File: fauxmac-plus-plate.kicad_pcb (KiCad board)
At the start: 2 copper layers, 86.5 x 89 mm, 4 parts

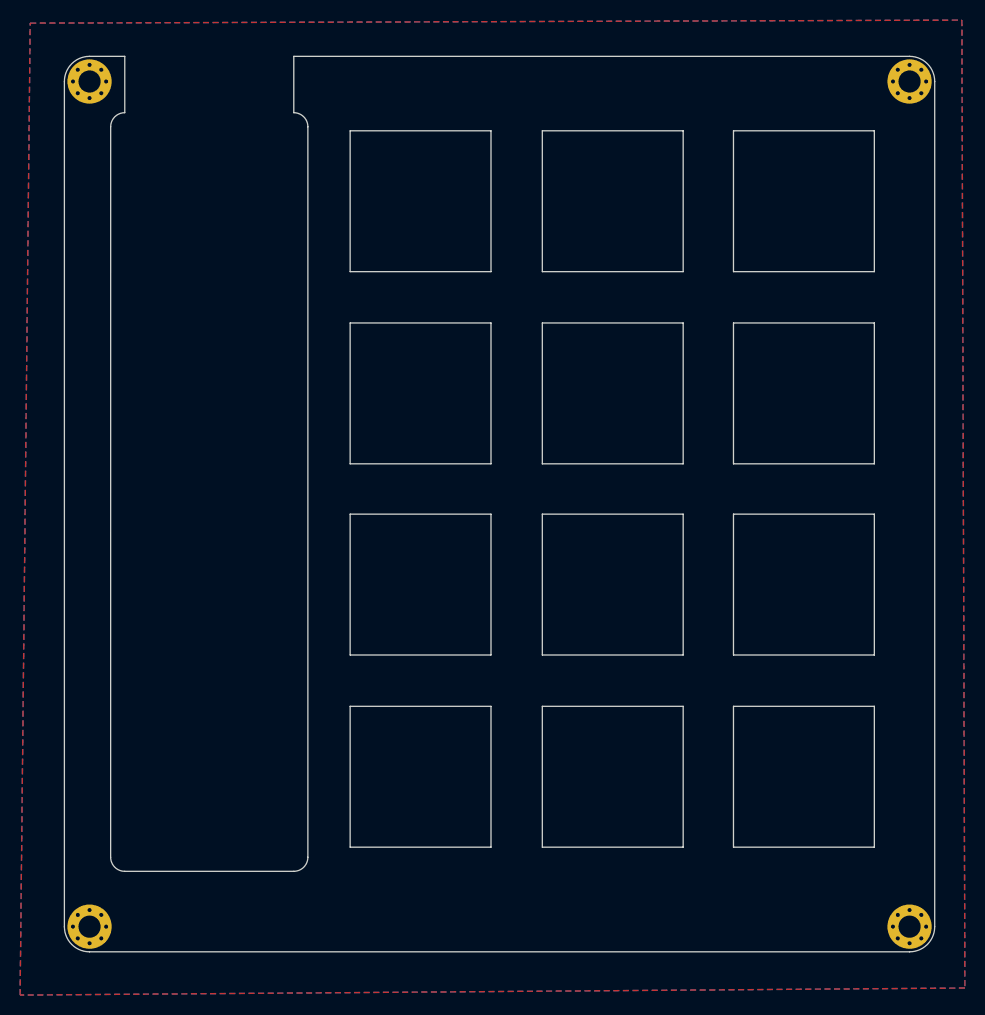
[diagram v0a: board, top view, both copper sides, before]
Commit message: update mounting points, fix plate
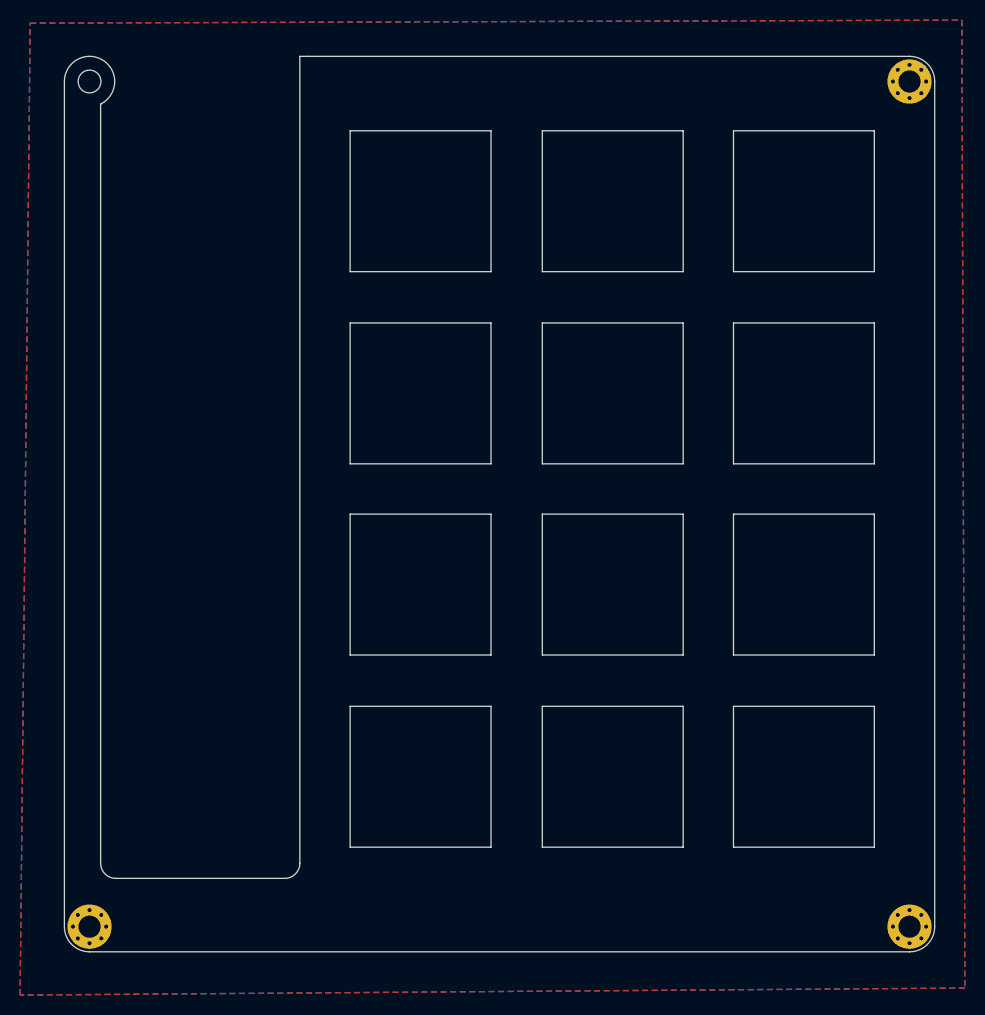
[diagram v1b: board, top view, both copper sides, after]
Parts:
- removed the   at (126.5, 28.5)
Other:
- outline, holes or cut-outs redrawn
